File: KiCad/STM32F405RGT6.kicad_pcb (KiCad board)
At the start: 4 copper layers, 101.6 x 101.6 mm, 54 parts, among them J1 Conn_02x05_Odd_Even, J2 USB_C_Receptacle_USB2.0, J3 Conn_02x32_Odd_Even, J4 Conn_02x20_Odd_Even, SW1 TS-1187A, SW2 TS-1187A, U1 AMS1117-3.3, U2 M24C02-RMN, U3 STM32F405RGTx, U4 SRV05-4, Y1 16MHz

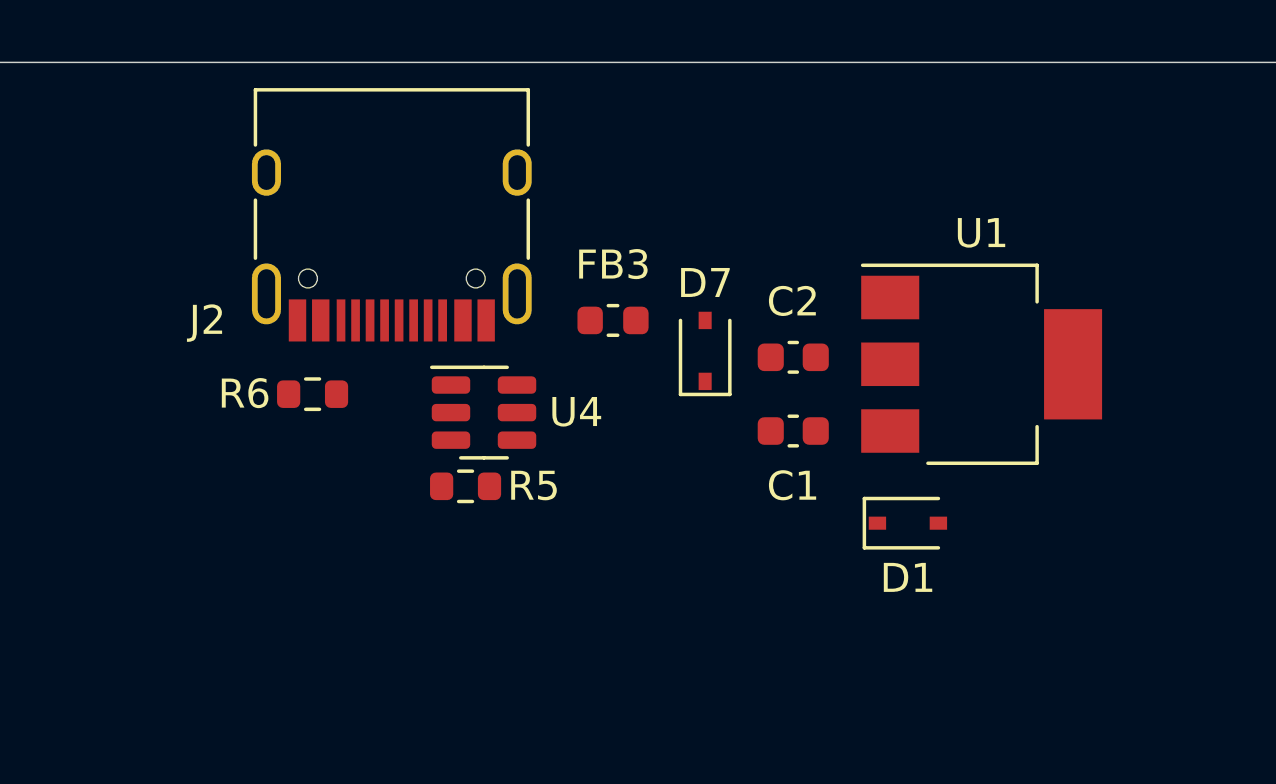
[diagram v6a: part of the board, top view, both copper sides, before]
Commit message: added USB 3D model and PTC fuse
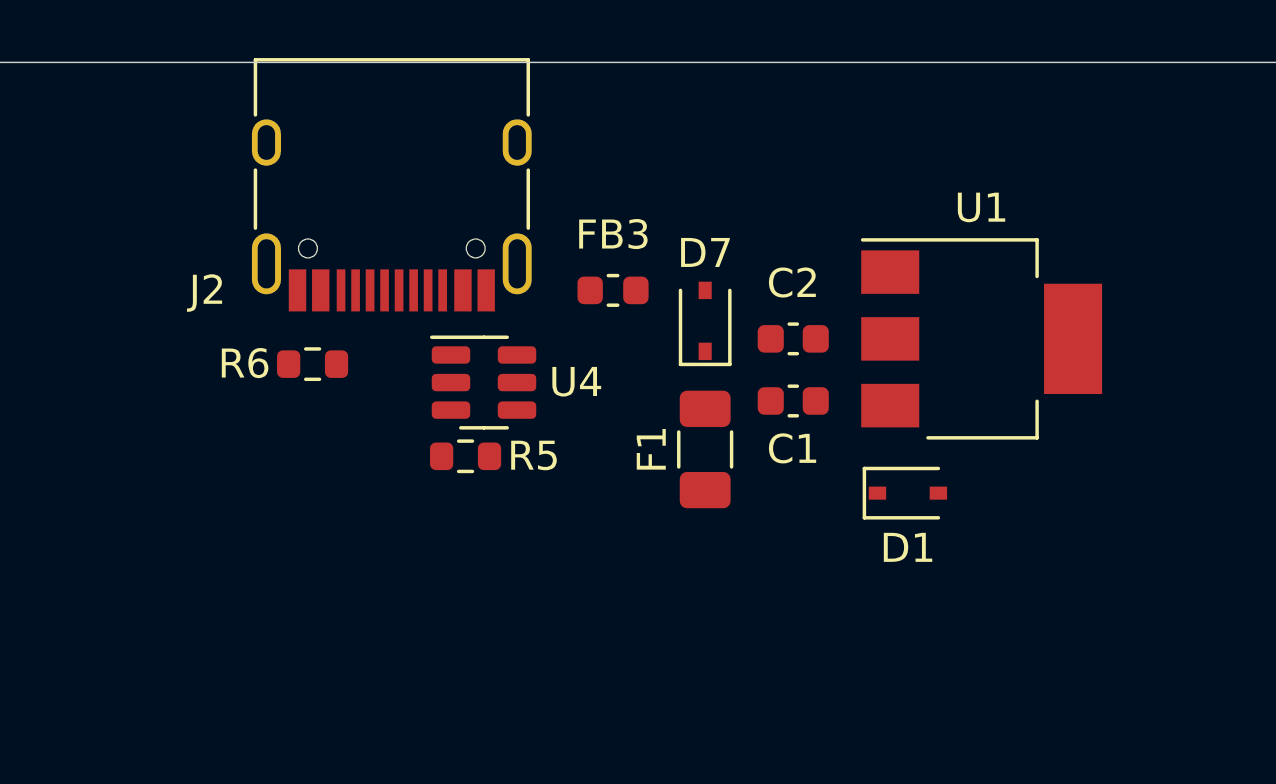
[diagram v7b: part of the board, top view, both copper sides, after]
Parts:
- added F1: 500mA, Fuse:Fuse_1206_3216Metric, F.Cu at (155.7, 47.3)
- moved D1 1.04 mm to (162.7, 48.8)
- moved FB3 1.04 mm to (152.5, 41.8)
- moved R6 1.04 mm to (142.2, 44.4)
- moved C1 1.03 mm to (158.8, 45.6), turned to 180 degrees
- moved D7 1.03 mm to (155.7, 42.9)
- moved J2 1.03 mm to (144.9, 37.8)
- moved R5 1.03 mm to (147.5, 47.5)
- moved U4 1.03 mm to (148.1, 45.0)
- moved U1 0.88 mm to (165.2, 43.5)
- moved C2 0.63 mm to (158.8, 43.5)
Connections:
- D7 pad 1: +5V -> Net-(D7-Pad1)
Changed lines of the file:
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@@
   (net 124 "NRST")
   (net 125 "+3V3")
+  (net 126 "Net-(D7-Pad1)")
   (footprint "MEP_TEMPLATE:Scope_GND" locked (layer "F.Cu")
     (at 191.91 50.47 90)
@@
     )
   )
+  (footprint "Fuse:Fuse_1206_3216Metric" (layer "F.Cu")
+    (at 155.715 47.295 90)
+    (descr "Fuse SMD 1206 (3216 Metric), square (rectangular) end terminal, IPC_7351 nominal, (Body size source: http://www.tortai-tech.com/upload/download/2011102023233369053.pdf), generated with kicad-footprint-generator")
+    (tags "fuse")
+    (property "JLCPCB Part #" "C720075")
+    (property "Part Number" "JK-nSMD050-30")
+    (property "Sheetfile" "STM32F405RGT6.kicad_sch")
+    (property "Sheetname" "")
+    (attr smd)
+    (fp_text reference "F1" (at 0 -1.82 90) (layer "F.SilkS")
+      (effects (font (size 1 1) (thickness 0.15)))
+    )
+    (fp_text value "500mA" (at 0 1.82 90) (layer "F.Fab")
+      (effects (font (size 1 1) (thickness 0.15)))
+    )
+    (fp_text user "${REFERENCE}" (at 0 0 90) (layer "F.Fab")
+      (effects (font (size 0.8 0.8) (thickness 0.12)))
+    )
+    (fp_line (start -0.602064 0.91) (end 0.602064 0.91) (layer "F.SilkS") (width 0.12))
+    (fp_line (start -0.602064 -0.91) (end 0.602064 -0.91) (layer "F.SilkS") (width 0.12))
+    (fp_line (start 2.28 -1.12) (end 2.28 1.12) (layer "F.CrtYd") (width 0.05))
+    (fp_line (start 2.28 1.12) (end -2.28 1.12) (layer "F.CrtYd") (width 0.05))
+    (fp_line (start -2.28 -1.12) (end 2.28 -1.12) (layer "F.CrtYd") (width 0.05))
+    (fp_line (start -2.28 1.12) (end -2.28 -1.12) (layer "F.CrtYd") (width 0.05))
+    (fp_line (start 1.6 0.8) (end -1.6 0.8) (layer "F.Fab") (width 0.1))
+    (fp_line (start -1.6 0.8) (end -1.6 -0.8) (layer "F.Fab") (width 0.1))
+    (fp_line (start 1.6 -0.8) (end 1.6 0.8) (layer "F.Fab") (width 0.1))
+    (fp_line (start -1.6 -0.8) (end 1.6 -0.8) (layer "F.Fab") (width 0.1))
+    (pad "1" smd roundrect (at -1.4 0 90) (size 1.25 1.75) (layers "F.Cu" "F.Paste" "F.Mask") (roundrect_rratio 0.2)
+      (net 4 "+5V") (pintype "passive"))
+    (pad "2" smd roundrect (at 1.4 0 90) (size 1.25 1.75) (layers "F.Cu" "F.Paste" "F.Mask") (roundrect_rratio 0.2)
+      (net 126 "Net-(D7-Pad1)") (pintype "passive"))
+    (model "${KICAD6_3DMODEL_DIR}/Fuse.3dshapes/Fuse_1206_3216Metric.wrl"
+      (offset (xyz 0 0 0))
+      (scale (xyz 1 1 1))
+      (rotate (xyz 0 0 0))
+    )
+  )
   (footprint "Button_Switch_SMD:SW_SPST_SKQG_WithStem" (layer "F.Cu")
     (at 155.08 130.48)
@@
   )
   (footprint "Package_TO_SOT_SMD:SOT-23-6" (layer "F.Cu")
-    (at 148.095 46.025)
+    (at 148.095 44.99)
     (descr "SOT, 6 Pin (https://www.jedec.org/sites/default/files/docs/Mo-178c.PDF variant AB), generated with kicad-footprint-generator ipc_gullwing_generator.py")
     (tags "SOT TO_SOT_SMD")
@@
   )
   (footprint "Capacitor_SMD:C_0603_1608Metric" (layer "F.Cu")
-    (at 158.75 44.12 180)
+    (at 158.75 43.485 180)
     (descr "Capacitor SMD 0603 (1608 Metric), square (rectangular) end terminal, IPC_7351 nominal, (Body size source: IPC-SM-782 page 76, https://www.pcb-3d.com/wordpress/wp-content/uploads/ipc-sm-782a_amendment_1_and_2.pdf), generated with kicad-footprint-generator")
     (tags "capacitor")
@@
   )
   (footprint "Resistor_SMD:R_0603_1608Metric" (layer "F.Cu")
-    (at 142.19 45.39)
+    (at 142.19 44.355)
     (descr "Resistor SMD 0603 (1608 Metric), square (rectangular) end terminal, IPC_7351 nominal, (Body size source: IPC-SM-782 page 72, https://www.pcb-3d.com/wordpress/wp-content/uploads/ipc-sm-782a_amendment_1_and_2.pdf), generated with kicad-footprint-generator")
     (tags "resistor")
@@
   )
   (footprint "Inductor_SMD:L_0603_1608Metric" (layer "F.Cu")
-    (at 152.54 42.85 180)
+    (at 152.54 41.815 180)
     (descr "Inductor SMD 0603 (1608 Metric), square (rectangular) end terminal, IPC_7351 nominal, (Body size source: http://www.tortai-tech.com/upload/download/2011102023233369053.pdf), generated with kicad-footprint-generator")
     (tags "inductor")
@@
   )
   (footprint "Connector_USB:USB_C_Receptacle_HRO_TYPE-C-31-M-12" (layer "F.Cu")
-    (at 144.92 38.805 180)
+    (at 144.92 37.77 180)
     (descr "USB Type-C receptacle for USB 2.0 and PD, http://www.krhro.com/uploads/soft/180320/1-1P320120243.pdf")
     (tags "usb usb-c 2.0 pd")
@@
     (pad "S1" thru_hole oval (at 4.32 1.05 180) (size 1 1.6) (drill oval 0.6 1.2) (layers *.Cu *.Mask)
       (net 104 "unconnected-(J2-PadS1)") (pinfunction "SHIELD") (pintype "passive+no_connect"))
-    (model "${KICAD6_3DMODEL_DIR}/Connector_USB.3dshapes/USB_C_Receptacle_HRO_TYPE-C-31-M-12.wrl"
-      (offset (xyz 0 0 0))
-      (scale (xyz 1 1 1))
-      (rotate (xyz 0 0 0))
+    (model "${KIPRJMOD}/Libraries/TYPE-C-31-M-12.step"
+      (offset (xyz -4.475 -3.65 0))
+      (scale (xyz 1 1 1))
+      (rotate (xyz -90 0 0))
     )
   )
   (footprint "Package_TO_SOT_SMD:SOT-223-3_TabPin2" (layer "F.Cu")
-    (at 165.24 44.36)
+    (at 165.24 43.485)
     (descr "module CMS SOT223 4 pins")
     (tags "CMS SOT")
@@
   )
   (footprint "Resistor_SMD:R_0603_1608Metric" (layer "F.Cu")
-    (at 147.46 48.565 180)
+    (at 147.46 47.53 180)
     (descr "Resistor SMD 0603 (1608 Metric), square (rectangular) end terminal, IPC_7351 nominal, (Body size source: IPC-SM-782 page 72, https://www.pcb-3d.com/wordpress/wp-content/uploads/ipc-sm-782a_amendment_1_and_2.pdf), generated with kicad-footprint-generator")
     (tags "resistor")
@@
   )
   (footprint "Capacitor_SMD:C_0603_1608Metric" (layer "F.Cu")
-    (at 158.75 46.66)
+    (at 158.75 45.625 180)
     (descr "Capacitor SMD 0603 (1608 Metric), square (rectangular) end terminal, IPC_7351 nominal, (Body size source: IPC-SM-782 page 76, https://www.pcb-3d.com/wordpress/wp-content/uploads/ipc-sm-782a_amendment_1_and_2.pdf), generated with kicad-footprint-generator")
     (tags "capacitor")
@@
     (property "Sheetname" "")
     (attr smd)
-    (fp_text reference "C1" (at 0 1.905) (layer "F.SilkS")
+    (fp_text reference "C1" (at 0 -1.67) (layer "F.SilkS")
       (effects (font (size 1 1) (thickness 0.15)))
     )
@@
     (fp_line (start 0.8 -0.4) (end 0.8 0.4) (layer "F.Fab") (width 0.1))
     (fp_line (start -0.8 0.4) (end -0.8 -0.4) (layer "F.Fab") (width 0.1))
-    (pad "1" smd roundrect (at -0.775 0) (size 0.9 0.95) (layers "F.Cu" "F.Paste" "F.Mask") (roundrect_rratio 0.25)
+    (pad "1" smd roundrect (at -0.775 0 180) (size 0.9 0.95) (layers "F.Cu" "F.Paste" "F.Mask") (roundrect_rratio 0.25)
       (net 4 "+5V") (pintype "passive"))
-    (pad "2" smd roundrect (at 0.775 0) (size 0.9 0.95) (layers "F.Cu" "F.Paste" "F.Mask") (roundrect_rratio 0.25)
+    (pad "2" smd roundrect (at 0.775 0 180) (size 0.9 0.95) (layers "F.Cu" "F.Paste" "F.Mask") (roundrect_rratio 0.25)
       (net 1 "GND") (pintype "passive"))
     (model "${KICAD6_3DMODEL_DIR}/Capacitor_SMD.3dshapes/C_0603_1608Metric.wrl"
@@
   )
   (footprint "Diode_SMD:D_SOD-323" (layer "F.Cu")
-    (at 162.7 49.835)
+    (at 162.7 48.8)
     (descr "SOD-323")
     (tags "SOD-323")
@@
   )
   (footprint "Diode_SMD:D_SOD-323" (layer "F.Cu")
-    (at 155.715 43.9 90)
+    (at 155.715 42.865 90)
     (descr "SOD-323")
     (tags "SOD-323")
@@
     (fp_line (start 0.2 0) (end 0.45 0) (layer "F.Fab") (width 0.1))
     (pad "1" smd rect (at -1.05 0 90) (size 0.6 0.45) (layers "F.Cu" "F.Paste" "F.Mask")
-      (net 4 "+5V") (pinfunction "K") (pintype "passive"))
+      (net 126 "Net-(D7-Pad1)") (pinfunction "K") (pintype "passive"))
     (pad "2" smd rect (at 1.05 0 90) (size 0.6 0.45) (layers "F.Cu" "F.Paste" "F.Mask")
       (net 94 "Net-(D7-Pad2)") (pinfunction "A") (pintype "passive"))

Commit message: Updated Schematic and PCB
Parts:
- removed the C4 at (167.1, 130.5)
- removed the SW2 at (172.9, 130.5)
- added C1: 100nF, Capacitor_SMD:C_0603_1608Metric, F.Cu at (167.1, 130.5)
- added C6: 100nF, Capacitor_SMD:C_0603_1608Metric, F.Cu at (138.6, 96.8)
- added D8: LED_Small, LED_SMD:LED_0603_1608Metric, F.Cu at (167.0, 48.6)
- added R1: 10k, Resistor_SMD:R_0603_1608Metric, F.Cu at (178.6, 130.5)
- added R11: 1k, Resistor_SMD:R_0603_1608Metric, F.Cu at (171.0, 48.6)
- added R3: 10k, Resistor_SMD:R_0603_1608Metric, F.Cu at (160.8, 130.5)
- added R4: 5k1, Resistor_SMD:R_0603_1608Metric, F.Cu at (144.5, 100.6)
- added R5: 5k1, Resistor_SMD:R_0603_1608Metric, F.Cu at (144.5, 103.2)
- added SW1: TS-1187A, Button_Switch_SMD:SW_SPST_SKQG_WithStem, F.Cu at (172.9, 130.5)
- JP2: footprint Connector_PinHeader_2.54mm:PinHeader_1x02_P2.54mm_Vertical -> Jumper:SolderJumper-3_P1.3mm_Bridged12_RoundedPad1.0x1.5mm
- moved JP2 2.69 mm to (161.4, 81.6)
- moved C2 0.64 mm to (149.4, 130.5)
- moved D7 0.23 mm to (162.7, 48.6)
- renumbered C1 to C17, C2 to C18, C3 to C2, C5 to C3, C6 to C4, C7 to C5, C8 to C7, C9 to C8, C17 to C9, D4 to D1, D5 to D2, D6 to D3, D2 to D4, D3 to D5, D7 to D6, D1 to D7, R6 to R10, R1 to R2, R2 to R6, R3 to R7, R4 to R8, R5 to R9, SW1 to SW2, U2 to U1, U3 to U2, U1 to U3
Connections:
- C2 pad 1: +3V3 -> /NRST_SW
- D3 pad 4: TODO -> GPIO19~
- FB2 pad 2: +3.3VA -> Net-(FB2-Pad2)
- JP2 pad 2: +3.3VA -> Net-(FB2-Pad2)
- SW2 pad 2: +3V3 -> /NRST_SW
- U1 pad 4: unconnected-(U2-Pad4) -> GND
- U1 pad 8: unconnected-(U2-Pad8) -> +3V3
- U2 pad 7: +3V3 -> /NRST_SW
